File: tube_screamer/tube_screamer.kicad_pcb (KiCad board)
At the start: 2 copper layers, 80.9 x 100 mm, 67 parts, among them J1 Jack_6.35, J2 Jack_6.35, J6 Barrel_Jack_Switch, J7 Conn_01x01_Socket, J8 Conn_01x01_Socket, J9 top_panel_connector, P1 front_plate, P2 bottom_plate, Q1 MMBT5551, Q10 AO3401A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

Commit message: Checklist done, only layout left.
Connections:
- J9 pad 1: Net-(J9D-Pin_8) -> 9V
- J9 pad 10: 0 -> Net-(J9E-Pin_10)
- J9 pad 3: Net-(J9E-1) -> 0
- J9 pad 8: 9V -> Net-(J9D-Pin_8)
- R26 pad 1: Net-(J9E-1) -> Net-(J9E-Pin_10)
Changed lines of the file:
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@@
 	(net 38 "Net-(J9D-Pin_8)")
 	(net 39 "unconnected-(J9G-Pin_11-Pad11)")
-	(net 40 "Net-(J9E-1)")
+	(net 40 "Net-(J9E-Pin_10)")
 	(net 41 "unconnected-(J9G-Pin_15-Pad15)")
 	(net 42 "unconnected-(J9G-Pin_13-Pad13)")
@@
 			(layers "F.Cu" "F.Mask" "F.Paste")
 			(roundrect_rratio 0.25)
-			(net 40 "Net-(J9E-1)")
+			(net 40 "Net-(J9E-Pin_10)")
 			(pintype "passive")
 		)
@@
 			(remove_unused_layers no)
 			(roundrect_rratio 0.147059)
-			(net 38 "Net-(J9D-Pin_8)")
-			(pinfunction "Pin_8")
+			(net 12 "9V")
+			(pinfunction "VCC")
 			(pintype "passive")
 		)
@@
 			(layers "*.Cu" "*.Mask")
 			(remove_unused_layers no)
-			(net 40 "Net-(J9E-1)")
-			(pinfunction "1")
+			(net 1 "0")
+			(pinfunction "GND")
 			(pintype "passive")
 		)
@@
 			(layers "*.Cu" "*.Mask")
 			(remove_unused_layers no)
-			(net 12 "9V")
-			(pinfunction "VCC")
+			(net 38 "Net-(J9D-Pin_8)")
+			(pinfunction "Pin_8")
 			(pintype "passive")
 		)
@@
 			(layers "*.Cu" "*.Mask")
 			(remove_unused_layers no)
-			(net 1 "0")
-			(pinfunction "GND")
+			(net 40 "Net-(J9E-Pin_10)")
+			(pinfunction "Pin_10")
 			(pintype "passive")
 		)

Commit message: 2.2 kOhm LED resistance.
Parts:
- R26, R28: value 1k -> 2.2k
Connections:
- R26 pad 1: Net-(J9E-Pin_10) -> 9V
- R26 pad 2: 9V -> Net-(J9E-Pin_10)
- R28 pad 1: Net-(J9D-Pin_8) -> /RED_LED
- R28 pad 2: /RED_LED -> Net-(J9D-Pin_8)
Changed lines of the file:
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@@
 			)
 		)
-		(property "Value" "1k"
+		(property "Value" "2.2k"
 			(at 0 1.43 0)
 			(layer "F.Fab")
@@
 			)
 		)
-		(property "LCSC" "C21190"
+		(property "LCSC" "C4190"
 			(at 0 0 0)
 			(unlocked yes)
@@
 			(layers "F.Cu" "F.Mask" "F.Paste")
 			(roundrect_rratio 0.25)
-			(net 38 "Net-(J9D-Pin_8)")
+			(net 48 "/RED_LED")
 			(pintype "passive")
 		)
@@
 			(layers "F.Cu" "F.Mask" "F.Paste")
 			(roundrect_rratio 0.25)
-			(net 48 "/RED_LED")
+			(net 38 "Net-(J9D-Pin_8)")
 			(pintype "passive")
 		)
@@
 			)
 		)
-		(property "Value" "1k"
+		(property "Value" "2.2k"
 			(at 0 1.43 0)
 			(layer "F.Fab")
@@
 			)
 		)
-		(property "LCSC" "C21190"
+		(property "LCSC" "C4190"
 			(at 0 0 0)
 			(unlocked yes)
@@
 			(layers "F.Cu" "F.Mask" "F.Paste")
 			(roundrect_rratio 0.25)
-			(net 40 "Net-(J9E-Pin_10)")
+			(net 12 "9V")
 			(pintype "passive")
 		)
@@
 			(layers "F.Cu" "F.Mask" "F.Paste")
 			(roundrect_rratio 0.25)
-			(net 12 "9V")
+			(net 40 "Net-(J9E-Pin_10)")
 			(pintype "passive")
 		)

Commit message: dafsd
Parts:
- J9: footprint Connector_IDC:IDC-Header_2x08_P2.54mm_Vertical -> pedale:IDC-Header_2x08_P2.54mm_Vertical
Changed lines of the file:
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@@
 		)
 	)
-	(footprint "Connector_IDC:IDC-Header_2x08_P2.54mm_Vertical"
+	(footprint "pedale:IDC-Header_2x08_P2.54mm_Vertical"
 		(locked yes)
 		(layer "F.Cu")
@@
 		)
 		(fp_text user "${REFERENCE}"
-			(at 1.27 8.89 0)
+			(at 1.27 8.89 180)
 			(layer "F.Fab")
 			(effects
@@
 			)
 		)
+		(model "${KIPRJMOD}/../pedale.pretty/IDC_female_16_no_strain.step"
+			(offset
+				(xyz 1.5 -8.9 9.5)
+			)
+			(scale
+				(xyz 1 1 1)
+			)
+			(rotate
+				(xyz -90 -0 -90)
+			)
+		)

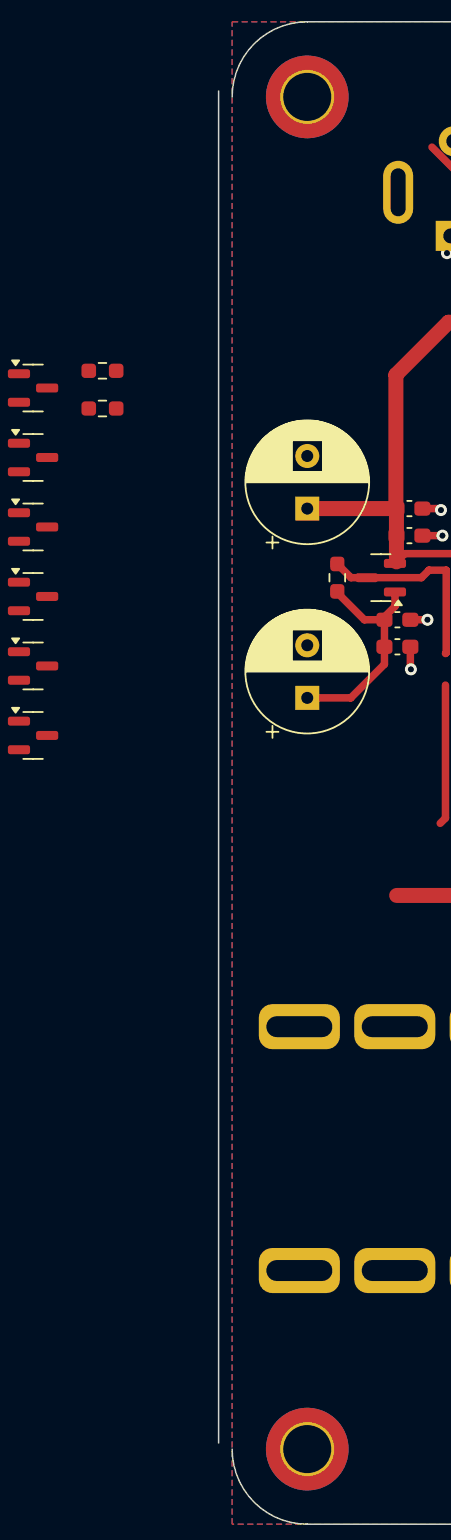
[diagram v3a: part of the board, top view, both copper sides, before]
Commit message: Updated 3D bodies.
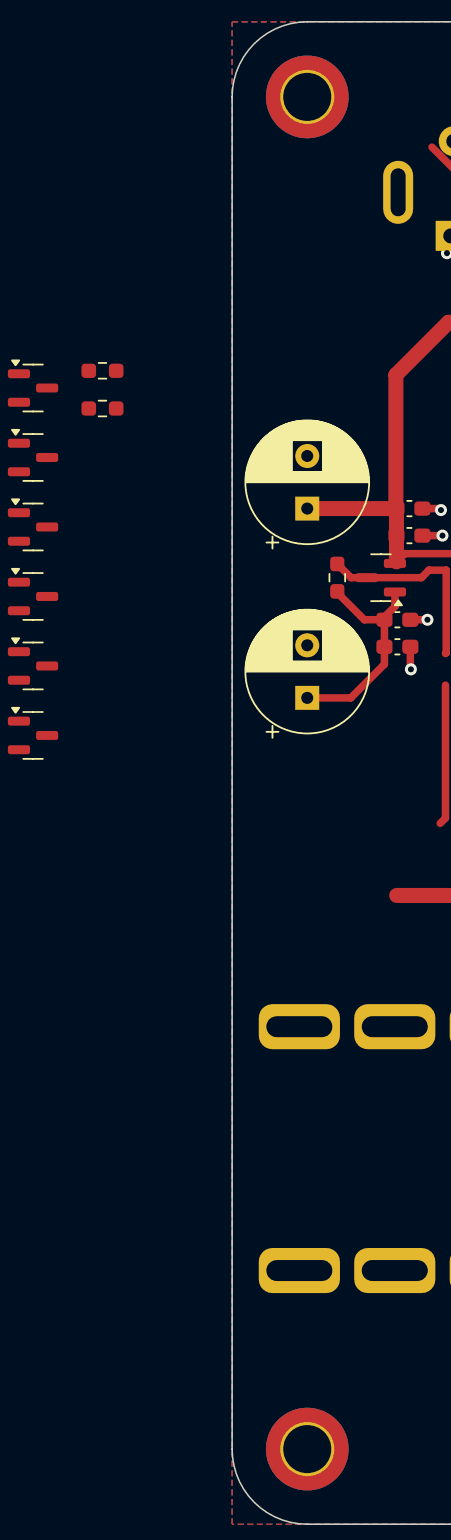
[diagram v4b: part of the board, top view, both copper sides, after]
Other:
- board size 80.9 x 100 mm -> 80 x 100 mm
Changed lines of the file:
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@@
 			(type default)
 		)
+		(locked yes)
 		(layer "Edge.Cuts")
 	)
@@
 			(type default)
 		)
+		(locked yes)
 		(layer "Edge.Cuts")
 	)
@@
 			(type default)
 		)
+		(locked yes)
 		(layer "Edge.Cuts")
 	)
@@
 			(type default)
 		)
+		(locked yes)
 		(layer "Edge.Cuts")
 	)
@@
 			(type default)
 		)
+		(locked yes)
 		(layer "Edge.Cuts")
 	)
@@
 			(type default)
 		)
+		(locked yes)
 		(layer "Edge.Cuts")
 	)
 	(gr_line
-		(start 49.1 54.6)
-		(end 49.1 144.6)
+		(start 50 55)
+		(end 50 145)
 		(stroke
 			(width 0.1)
 			(type default)
 		)
+		(locked yes)
 		(layer "Edge.Cuts")
 	)
@@
 			(type default)
 		)
+		(locked yes)
 		(layer "Edge.Cuts")
 	)

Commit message: Layout done.
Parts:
- moved R28 112.4 mm to (79.6, 123.4), turned to 90 degrees
- moved R47 73.9 mm to (86.3, 73.2), turned to -90 degrees
- moved R26 66.0 mm to (91.5, 73.2), turned to -90 degrees
- moved C6 52.9 mm to (90.0, 73.2), turned to 90 degrees
- moved R7 52.6 mm to (88.5, 73.2), turned to -90 degrees
- moved Q14 36.5 mm to (53.1, 64.9), turned to 180 degrees
- moved R22 31.3 mm to (80.8, 56.7)
- moved Q13 29.5 mm to (53.1, 68.3)
- moved C14 27.7 mm to (82.4, 56.7), turned to 90 degrees
- moved Q10 27.6 mm to (57.0, 64.9), turned to 180 degrees
- moved R23 23.3 mm to (84.0, 56.7), turned to 90 degrees
- moved Q8 22.9 mm to (57.0, 68.3)
- moved Q12 21.2 mm to (55.1, 77.7), turned to 90 degrees
- moved Q6 19.5 mm to (56.1, 72.2), turned to 90 degrees
- moved C8 15.9 mm to (68.2, 86.1), turned to 180 degrees
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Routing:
- net unconnected-(J2-PadTN): track 134.5 -> 0.00 mm, vias 2 -> 0
- net IN_CONNECT: track 0.00 -> 112.7 mm, vias 0 -> 2
- net /OUTPUT: track 8.90 -> 71.8 mm
- net unconnected-(J1-PadTN): track 61.7 -> 0.00 mm
- net /RED_LED: track 71.0 -> 12.2 mm
- net BAT-: track 17.5 -> 66.3 mm
- net Net-(J9D-Pin_8): track 0.00 -> 47.0 mm, vias 0 -> 2
- net /INPUT: track 8.34 -> 54.0 mm
- net /TON_HIGH: track 4.92 -> 44.8 mm
- net 4V5: track 73.0 -> 40.2 mm, vias 5 -> 0
- net /SW_ON: track 35.6 -> 67.9 mm
- net /OVD: track 12.7 -> 41.1 mm
- net BAT+: track 10.1 -> 34.8 mm
- net CONN-: track 0.00 -> 23.7 mm
- net Net-(D1-K): track 10.9 -> 33.4 mm, vias 0 -> 2
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
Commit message: kjflsad.
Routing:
- net 9V: track 191.1 -> 199.7 mm, vias 13 -> 10
- net IN_CONNECT: track 112.7 -> 114.9 mm
- net /OUTPUT: track 71.8 -> 72.8 mm
- net 0: vias 25 -> 48

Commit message: Done.
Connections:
- SW1 pad 4: 9V -> unconnected-(SW1B-A-Pad4)
- SW1 pad 6: unconnected-(SW1B-C-Pad6) -> 9V
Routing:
- net 9V: track 199.7 -> 180.6 mm
- net 0: vias 48 -> 47
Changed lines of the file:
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@@
 	(net 42 "unconnected-(J9G-Pin_13-Pad13)")
 	(net 43 "/INPUT")
-	(net 44 "unconnected-(SW1B-C-Pad6)")
+	(net 44 "unconnected-(SW1B-A-Pad4)")
 	(net 45 "/TON_HIGH")
 	(net 46 "Net-(J9B-Pin_7)")
@@
 			(remove_unused_layers no)
 			(roundrect_rratio 0.25)
-			(net 12 "9V")
+			(net 44 "unconnected-(SW1B-A-Pad4)")
 			(pinfunction "A")
-			(pintype "passive")
+			(pintype "passive+no_connect")
 			(thermal_bridge_angle 45)
 		)
@@
 			(remove_unused_layers no)
 			(roundrect_rratio 0.25)
-			(net 44 "unconnected-(SW1B-C-Pad6)")
+			(net 12 "9V")
 			(pinfunction "C")
-			(pintype "passive+no_connect")
+			(pintype "passive")
 			(thermal_bridge_angle 45)
 		)
@@
 	)
 	(via
-		(at 79.8 127.3)
-		(size 0.8)
-		(drill 0.4)
-		(layers "F.Cu" "B.Cu")
-		(free yes)
-		(net 1)
-	)
-	(via
 		(at 110.7 89.7)
 		(size 0.8)
@@
 	)
 	(segment
+		(start 78.1 125.500334)
+		(end 78.1 118.4)
+		(width 1)
+		(layer "F.Cu")
+		(net 12)
+	)
+	(segment
 		(start 91.5 67.807106)
 		(end 91.5 72.2875)
@@
 	)
 	(segment
-		(start 83.392031 133.6)
-		(end 90.746036 133.6)
+		(start 80.627222 59.442632)
+		(end 78.7375 59.442632)
 		(width 1)
 		(layer "F.Cu")
@@
 	)
 	(segment
-		(start 80.627222 59.442632)
-		(end 78.7375 59.442632)
+		(start 71.393792 58.806207)
+		(end 72.882206 57.317792)
 		(width 1)
 		(layer "F.Cu")
@@
 	)
 	(segment
-		(start 71.393792 58.806207)
-		(end 72.882206 57.317792)
+		(start 79.271475 128.328525)
+		(end 79.574251 128.631301)
 		(width 1)
 		(layer "F.Cu")
@@
 	)
 	(segment
+		(start 81.671475 129.5)
+		(end 82.9 129.5)
+		(width 1)
+		(layer "F.Cu")
+		(net 12)
+	)
+	(segment
 		(start 70.05 77.2)
 		(end 69.7 77.2)
@@
 	)
 	(segment
-		(start 94.593792 132.006207)
-		(end 97.1 129.5)
-		(width 1)
-		(layer "F.Cu")
-		(net 12)
-	)
-	(segment
 		(start 85.182862 51.274)
 		(end 88.213712 51.274)
@@
 	)
 	(segment
-		(start 78.1 128.307968)
-		(end 78.1 118.4)
-		(width 1)
-		(layer "F.Cu")
-		(net 12)
-	)
-	(segment
 		(start 69.8 73.55)
 		(end 69.8 62.653963)
@@
 	)
 	(arc
+		(start 79.574251 128.631301)
+		(mid 80.536465 129.274232)
+		(end 81.671475 129.5)
+		(width 1)
+		(layer "F.Cu")
+		(net 12)
+	)
+	(arc
 		(start 90.894934 58.342566)
 		(mid 91.000087 58.272304)
@@
 	)
 	(arc
-		(start 83.392031 133.6)
-		(mid 81.366858 133.197168)
-		(end 79.65 132.05)
-		(width 1)
-		(layer "F.Cu")
-		(net 12)
-	)
-	(arc
 		(start 80.627222 59.442632)
 		(mid 80.655073 59.437092)
@@
 	)
 	(arc
-		(start 74.6525 86.598536)
-		(mid 75.066713 88.680926)
-		(end 76.246292 90.446292)
+		(start 78.1 125.500334)
+		(mid 78.404456 127.030939)
+		(end 79.271475 128.328525)
 		(width 1)
 		(layer "F.Cu")
@@
 	)
 	(arc
-		(start 90.746036 133.6)
-		(mid 92.828426 133.185786)
-		(end 94.593792 132.006207)
+		(start 74.6525 86.598536)
+		(mid 75.066713 88.680926)
+		(end 76.246292 90.446292)
 		(width 1)
 		(layer "F.Cu")
@@
 		(width 1)
 		(layer "F.Cu")
-		(net 12)
-	)
-	(arc
-		(start 78.1 128.307968)
-		(mid 78.502831 130.333141)
-		(end 79.65 132.05)
-		(width 1)
-		(layer "F.Cu")

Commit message: Ready for production.
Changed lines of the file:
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@@
 			(outputformat 1)
 			(mirror no)
-			(drillshape 1)
+			(drillshape 0)
 			(scaleselection 1)
-			(outputdirectory "")
+			(outputdirectory "gerbers/")
 		)
 	)
@@
 			(at 1.27 -6.1 90)
 			(layer "F.SilkS")
+			(hide yes)
 			(effects
 				(font
